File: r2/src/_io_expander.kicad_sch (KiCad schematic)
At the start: 7 parts, among them U6 PCA9555PW

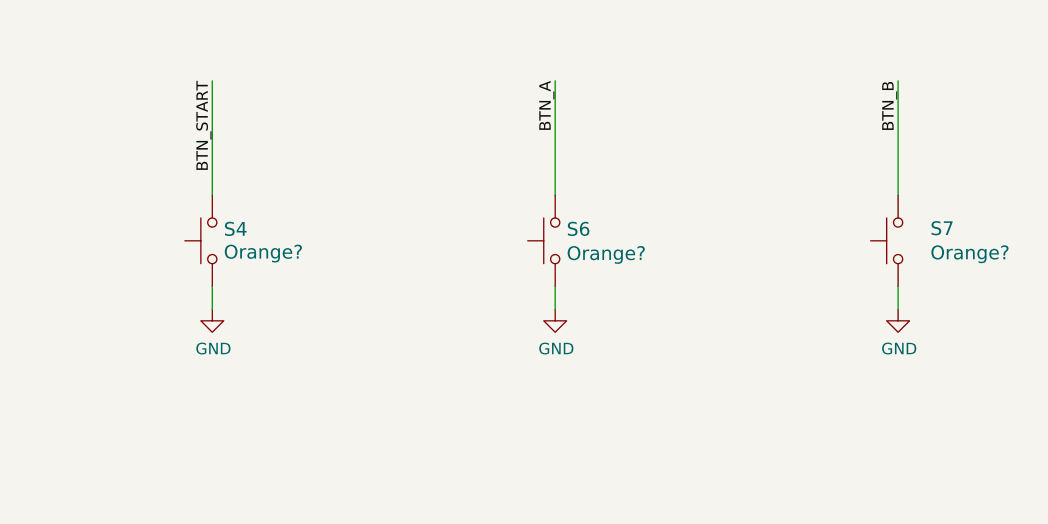
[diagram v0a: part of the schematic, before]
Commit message: Fix tactile switch symbols. By using a two-pin symbol rather than the truer 4-pin one, signals were shorted at the footprint
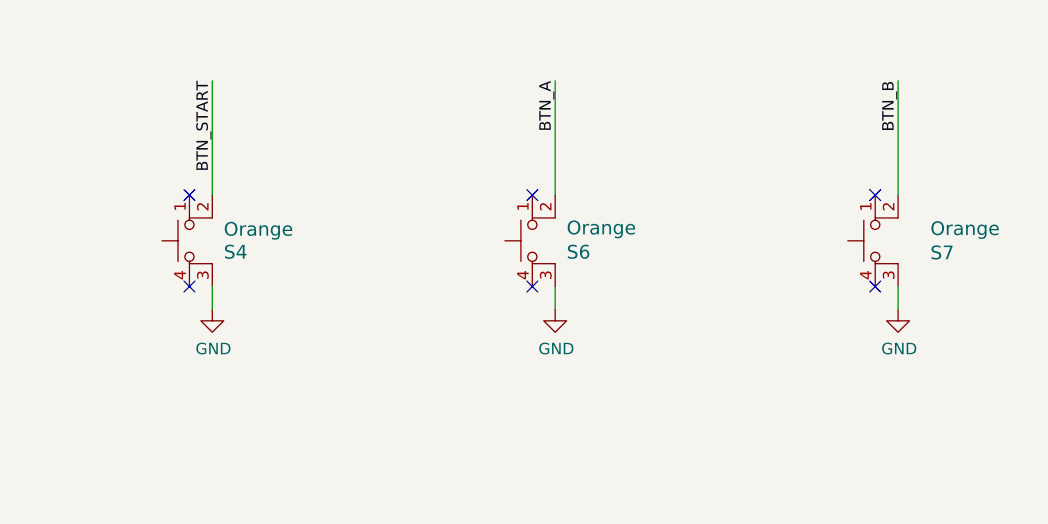
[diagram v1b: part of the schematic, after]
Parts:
- S4, S6, S7: value Orange? -> Orange; symbol Switch:SW_Push -> Switch:SW_MEC_5E
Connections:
- net GND: now also S4.3 (K), S6.3 (K), S7.3 (K); no longer S4.1, S6.1, S7.1
- no-connect marks 0 -> 6

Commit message: Set title block contents
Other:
- company: (none) -> Monad Gottfried Ltd. 2023
- title: (none) -> Troopers 23 Badge
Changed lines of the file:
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@@
 (kicad_sch (version 20230409) (generator eeschema)
   (paper "A4")
+  (title_block
+    (title "Troopers 23 Badge")
+    (rev "r2")
+    (company "Monad Gottfried Ltd. 2023")
+    (comment 1 "for ERNW Enno Rey Netzwerke GmbH")
+  )
   (junction (at 60.96 60.96) (diameter 0) (color 0 0 0 0)
   )
